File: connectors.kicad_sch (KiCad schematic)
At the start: 32 parts, among them J1 Conn_01x04, J10 Conn_02x02_Counter_Clockwise, J11 Conn_02x02_Counter_Clockwise, J12 Conn_02x02_Counter_Clockwise, J13 Conn_02x02_Counter_Clockwise, J14 Conn_02x02_Counter_Clockwise, J15 Conn_01x02, J16 Conn_01x02, J17 Conn_01x02, J18 Conn_01x02, J19 Conn_01x01, J20 Conn_01x01, J21 Conn_01x01, J22 Conn_01x01, J23 Conn_01x02, J24 Conn_01x02, J25 Conn_01x08, J26 Conn_01x08, J27 Conn_01x04, J3 Conn_01x04, J5 Conn_01x04, J7 Conn_02x02_Counter_Clockwise, J8 Conn_02x02_Counter_Clockwise, J9 Conn_02x02_Counter_Clockwise, P1 USB_C_Plug_USB2.0

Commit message: Fully connect all components
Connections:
- net CLUTCH-IN is gone; now on net TPS-IN: J25.3 (Pin_3)
- net COOLANT-IN: now also J25.5 (Pin_5); no longer J25.6 (Pin_6)
- net IAT-IN: now also J25.6 (Pin_6); no longer J25.2 (Pin_2)
- net O2-IN: now also J25.4 (Pin_4); no longer J25.5 (Pin_5)
- net TPS-IN: no longer J25.4 (Pin_4)
- net RAW-BARO-IN renamed BARO-HZ-IN
- net RAW-EXTRA-GPIO-10-A renamed EXTRA-GPIO-11-HZ-A
- net RAW-EXTRA-GPIO-11-A renamed EXTRA-GPIO-10-HZ-A
- net RAW-EXTRA-GPIO-12-A renamed EXTRA-GPIO-9-HZ-A
- net RAW-EXTRA-GPIO-9-A renamed EXTRA-GPIO-12-HZ-A
- net RAW-FLEX-IN renamed FLEX-HZ-IN
- net RAW-MAP-IN renamed MAP-HZ-IN
- new net CLUTCH-HZ-IN: J25.2 (Pin_2)
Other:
- moved on the sheet: TP1, TP2

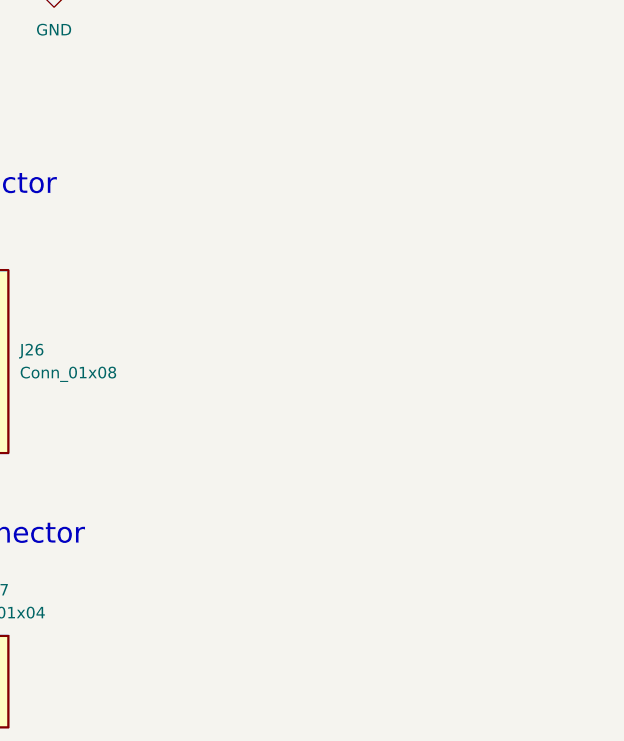
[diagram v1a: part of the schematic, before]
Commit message: Fix power traces width and add logo
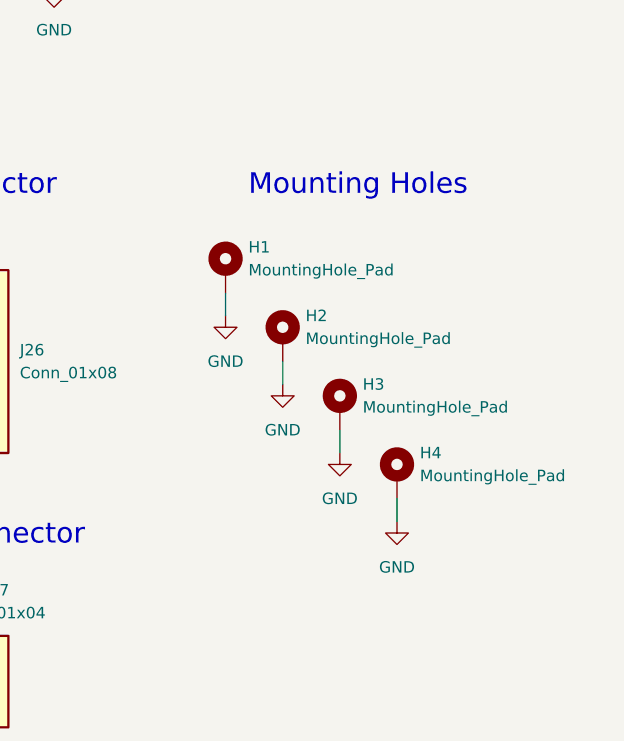
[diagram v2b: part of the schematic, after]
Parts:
- added H1, H2, H3, H4: MountingHole_Pad, MountingHole:MountingHole_4mm_Pad, symbol Mechanical:MountingHole_Pad
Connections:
- net GND: now also H1.1, H2.1, H3.1, H4.1
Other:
- note added: "Mounting Holes"

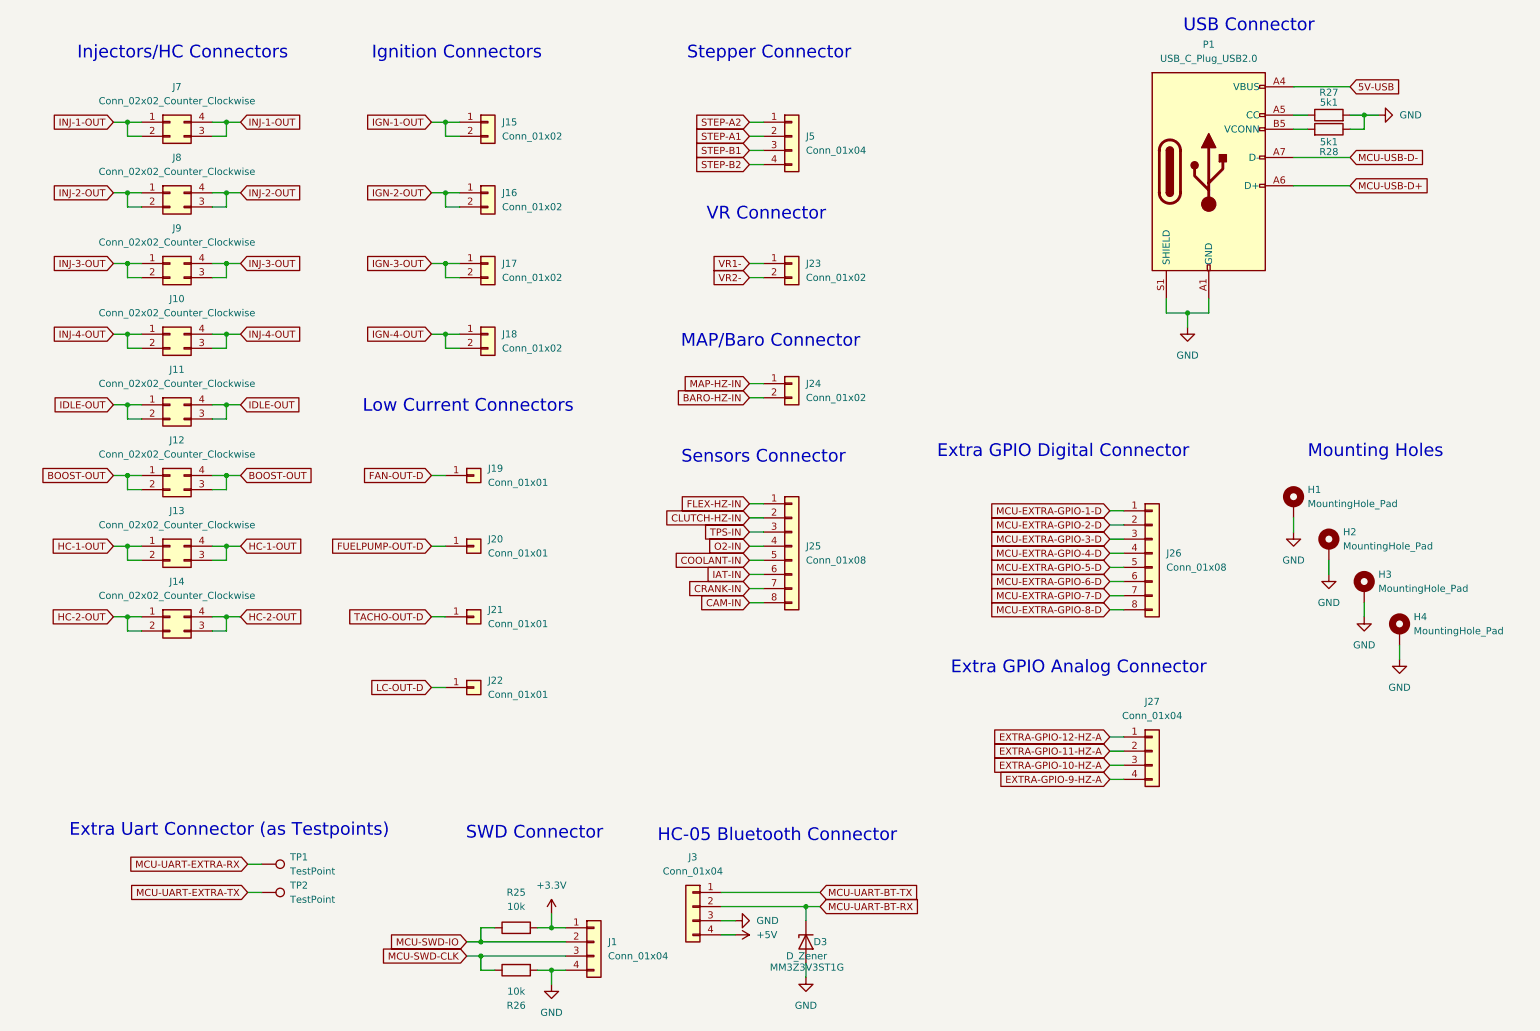
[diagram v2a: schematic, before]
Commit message: Updated reference layout
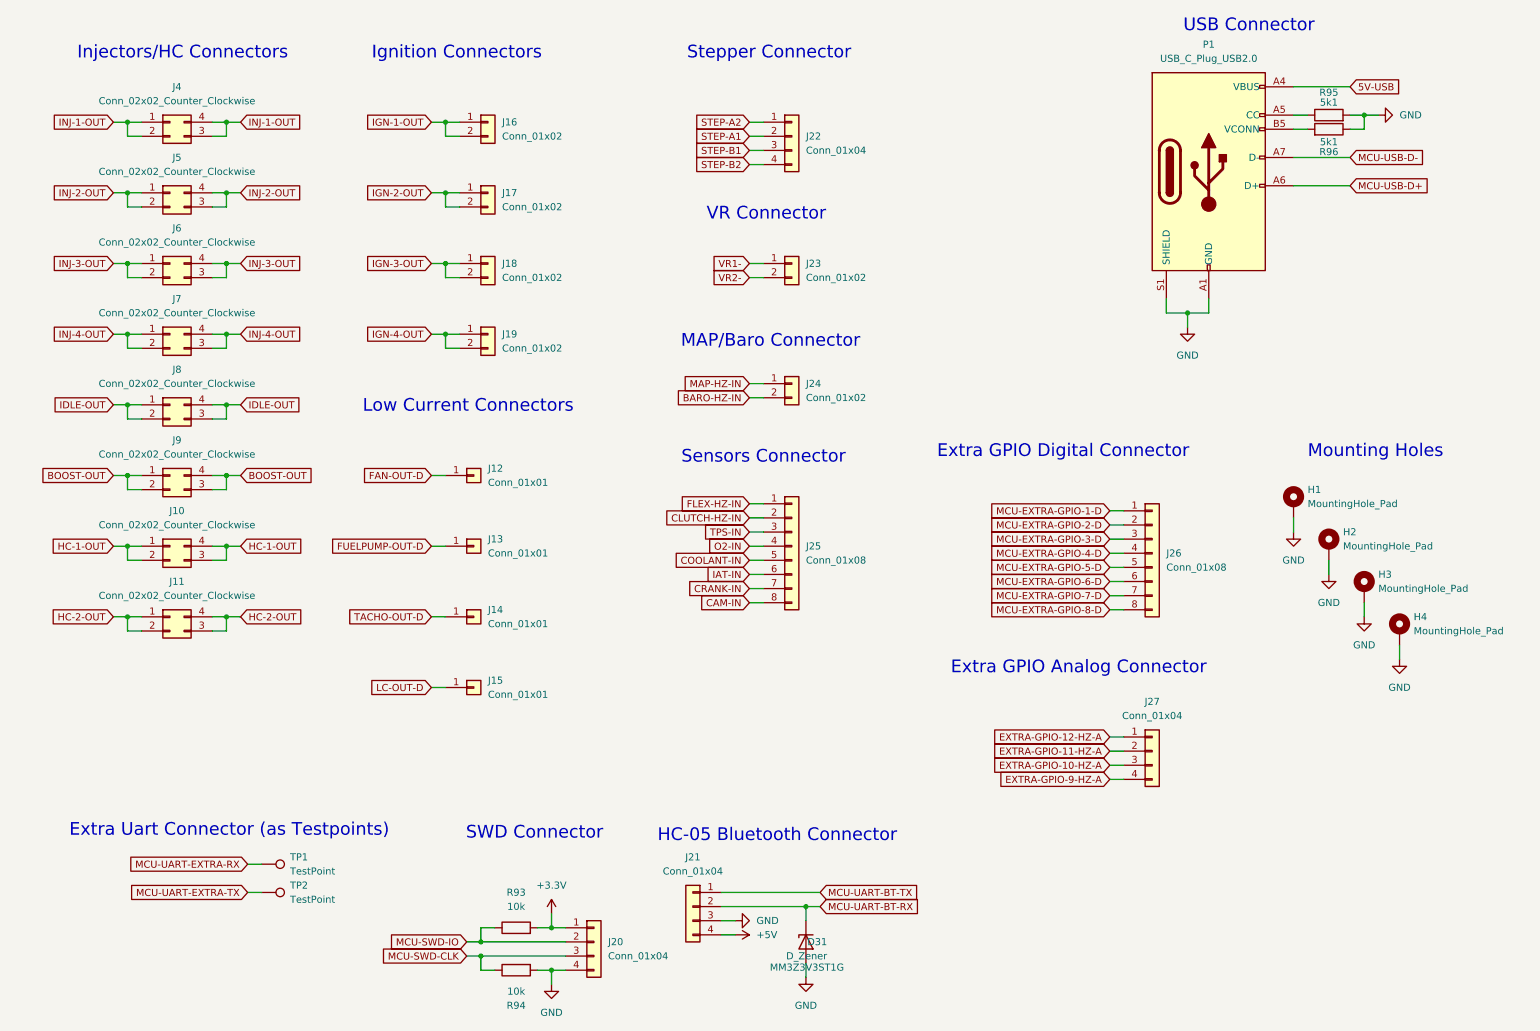
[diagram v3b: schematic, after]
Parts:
- renumbered D3 to D31, J13 to J10, J14 to J11, J19 to J12, J20 to J13, J21 to J14, J22 to J15, J15 to J16, J16 to J17, J17 to J18, J18 to J19, J1 to J20, J3 to J21, J5 to J22, J7 to J4, J8 to J5, J9 to J6, J10 to J7, J11 to J8, J12 to J9, R25 to R93, R26 to R94, R27 to R95, R28 to R96

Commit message: Change power layout, add low frequency crystal
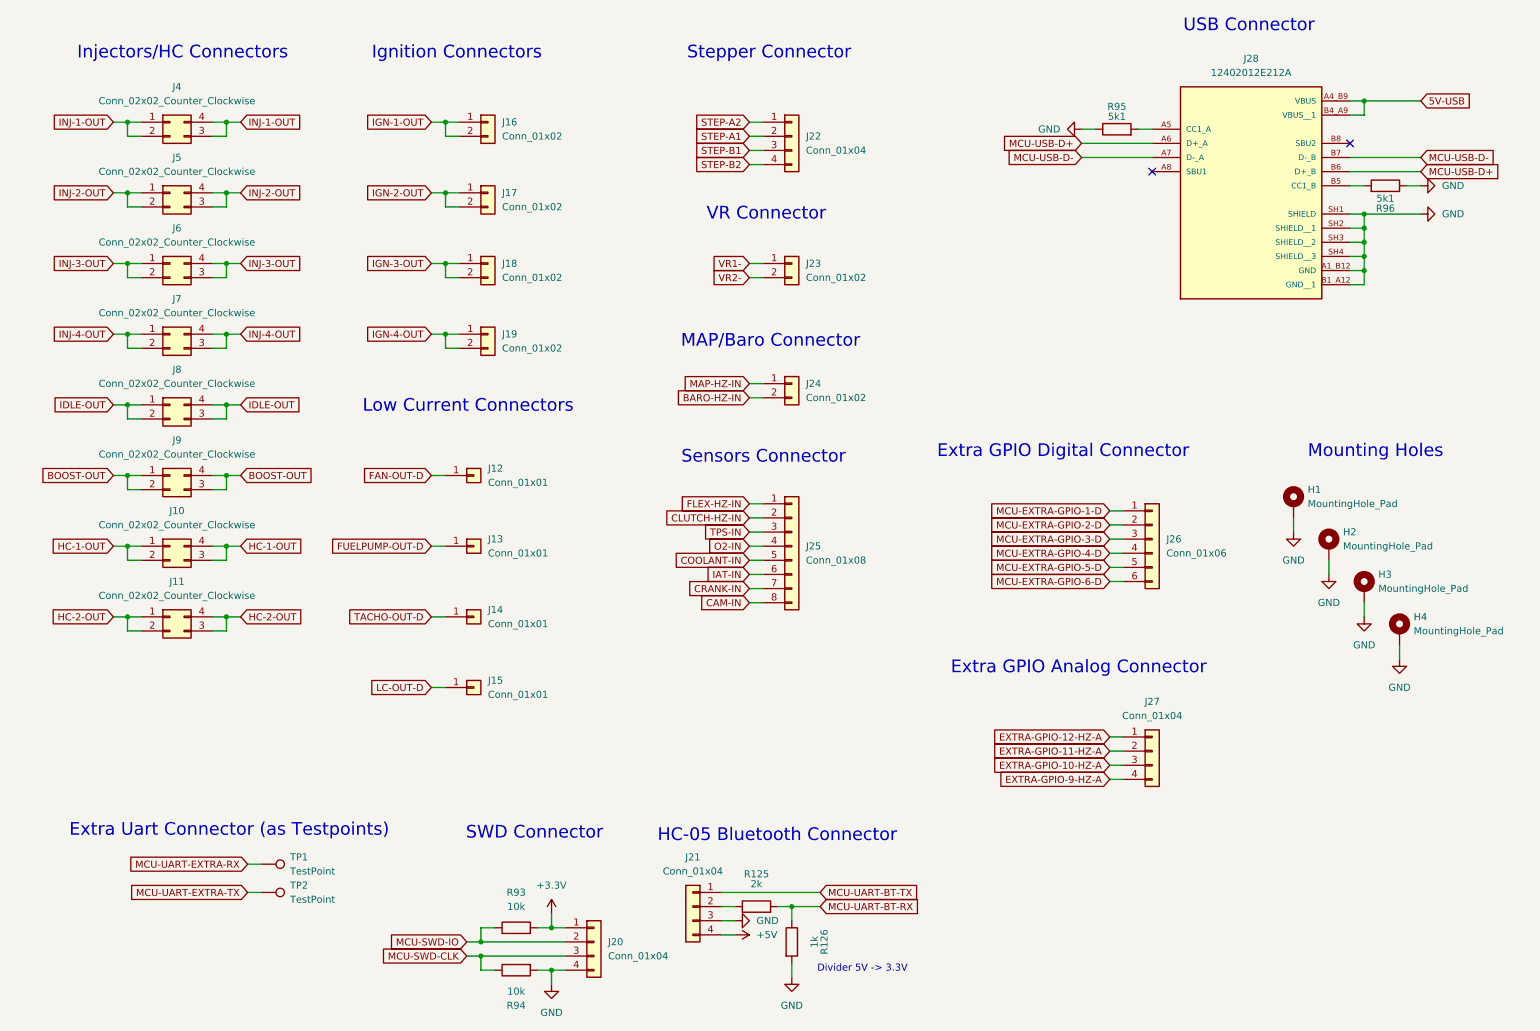
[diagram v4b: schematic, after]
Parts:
- removed D31: D_Zener, Diode_SMD:D_SOD-323, symbol Device:D_Zener
- removed J26: Conn_01x08, Connector_PinHeader_2.54mm:PinHeader_1x08_P2.54mm_Vertical, symbol Connector_Generic:Conn_01x08
- removed P1: USB_C_Plug_USB2.0, Connector_USB:USB_C_Receptacle_Palconn_UTC16-G, symbol Connector:USB_C_Plug_USB2.0
- added J26: Conn_01x06, Connector_PinHeader_2.54mm:PinHeader_1x06_P2.54mm_Vertical, symbol Connector_Generic:Conn_01x06
- added J28: 12402012E212A, Misc:AMPHENOL_12402012E212A, symbol Misc:12402012E212A
- added R125: 2k, Resistor_SMD:R_0805_2012Metric, symbol Device:R
- added R126: 1k, Resistor_SMD:R_0805_2012Metric, symbol Device:R
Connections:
- net 5V-USB: now also J28.A4_B9 (VBUS), J28.B4_A9 (VBUS__1)
- net GND: now also R95.1, J28.A1_B12 (GND), J28.B1_A12 (GND__1), J28.SH1 (SHIELD), J28.SH2 (SHIELD__1), J28.SH3 (SHIELD__2), J28.SH4 (SHIELD__3), R126.2; no longer R95.2
- net MCU-EXTRA-GPIO-1-D: now also J26.1 (Pin_1)
- net MCU-EXTRA-GPIO-2-D: now also J26.2 (Pin_2)
- net MCU-EXTRA-GPIO-3-D: now also J26.3 (Pin_3)
- net MCU-EXTRA-GPIO-4-D: now also J26.4 (Pin_4)
- net MCU-EXTRA-GPIO-5-D: now also J26.5 (Pin_5)
- net MCU-EXTRA-GPIO-6-D: now also J26.6 (Pin_6)
- net MCU-UART-BT-RX: now also R125.2, R126.1; no longer J21.2 (Pin_2)
- net MCU-USB-D+: now also J28.A6 (D+_A), J28.B6 (D+_B)
- net MCU-USB-D-: now also J28.A7 (D-_A), J28.B7 (D-_B)
- net at R96.2: now also J28.B5 (CC1_B)
- new net: J21.2 (Pin_2), R125.1
- new net: J28.A5 (CC1_A), R95.2
- no-connect marks 0 -> 2
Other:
- note added: "Divider 5V -> 3.3V"
- moved on the sheet: R95, R96
